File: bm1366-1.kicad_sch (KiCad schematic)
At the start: 56 parts, among them U1 25MHz, U13 ADP171AUJ-R7, U14 BM1366_mode1, U23 ADP171AUJ-R7

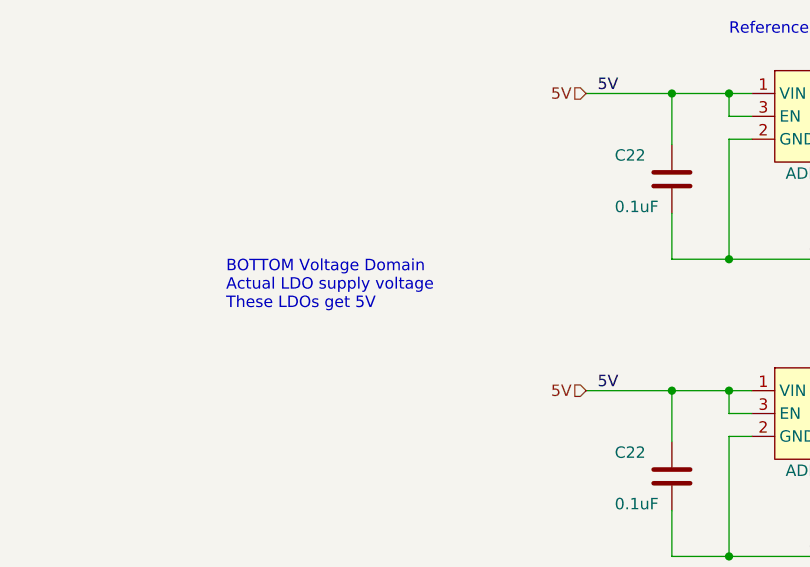
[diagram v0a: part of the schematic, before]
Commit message: add 1v8 LDO and consolidate voltage level translators
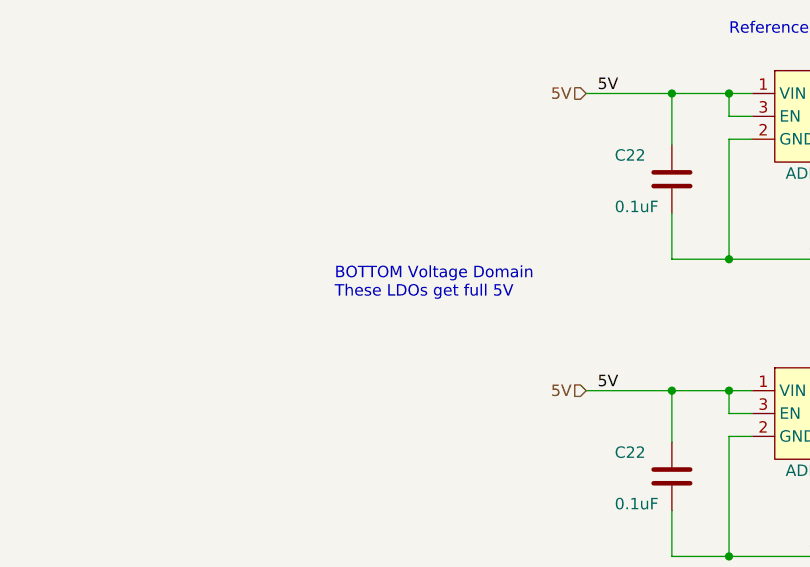
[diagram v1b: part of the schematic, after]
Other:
- note added: "BOTTOM Voltage Domain These LDOs get full 5V"
- note removed: "BOTTOM Voltage Domain Actual LDO supply voltage These LDOs get 5V"
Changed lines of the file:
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@@
     (effects (font (size 1.27 1.27)) (justify left bottom))
   )
-  (text "BOTTOM Voltage Domain\nActual LDO supply voltage\nThese LDOs get 5V"
-    (at 38.1 167.64 0)
+  (text "BOTTOM Voltage Domain\nThese LDOs get full 5V" (at 50.165 166.37 0)
     (effects (font (size 1.27 1.27)) (justify left bottom))
   )

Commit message: Resolved all unconnected pins, re-annotated, reviewed for layout
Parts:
- added TP13 (x4): TestPoint, TestPoint:TestPoint_Pad_D1.5mm, symbol Connector:TestPoint
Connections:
- net TEMP_N1: now also TP13.1
- net TEMP_N2: now also TP13.1
- net TEMP_P1: now also TP13.1
- net TEMP_P2: now also TP13.1
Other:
- moved on the sheet: R6

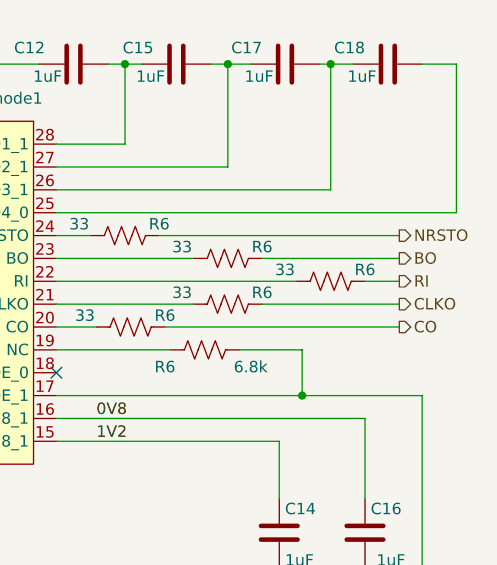
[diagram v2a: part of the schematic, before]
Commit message: replace Q5 with BSS123
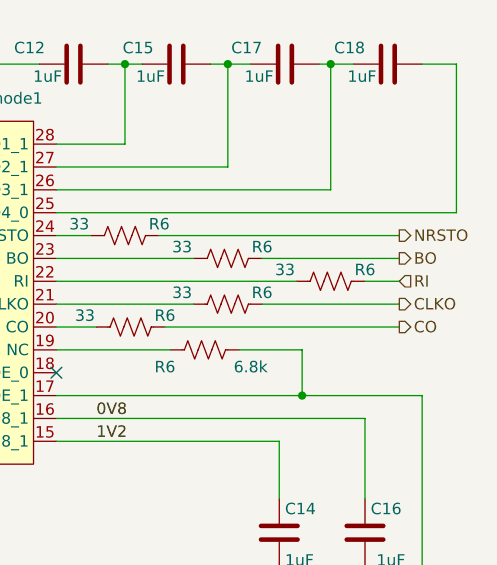
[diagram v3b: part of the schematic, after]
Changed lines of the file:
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@@
     (effects (font (size 1.27 1.27)) (justify right))
   )
-  (hierarchical_label "RI" (shape output) (at 256.54 90.17 0) (fields_autoplaced)
+  (hierarchical_label "RI" (shape input) (at 256.54 90.17 0) (fields_autoplaced)
     (effects (font (size 1.27 1.27)) (justify left))
   )

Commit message: Rough parts placement
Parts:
- TP13: footprint TestPoint:TestPoint_Pad_D1.5mm -> TestPoint:TestPoint_Pad_D1.0mm
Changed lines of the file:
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@@
     (effects (font (size 1.27 1.27)) (justify left bottom))
   )
-  (label "VDD" (at 202.565 66.04 0) (fields_autoplaced)
+  (label "VDD1" (at 202.565 66.04 0) (fields_autoplaced)
     (effects (font (size 1.27 1.27)) (justify left bottom))
   )
@@
     (effects (font (size 1.27 1.27)) (justify left bottom))
   )
-  (label "VDD" (at 74.295 66.04 0) (fields_autoplaced)
+  (label "VDD1" (at 74.295 66.04 0) (fields_autoplaced)
     (effects (font (size 1.27 1.27)) (justify left bottom))
   )
@@
     (effects (font (size 1.27 1.27)) (justify left bottom))
   )
-  (label "VDD" (at 165.735 146.685 0) (fields_autoplaced)
+  (label "VDD1" (at 165.735 146.685 0) (fields_autoplaced)
     (effects (font (size 1.27 1.27)) (justify left bottom))
   )
@@
       (effects (font (size 1.27 1.27)) (justify left) hide)
     )
-    (property "Footprint" "TestPoint:TestPoint_Pad_D1.5mm" (at 136.525 138.43 0)
+    (property "Footprint" "TestPoint:TestPoint_Pad_D1.0mm" (at 136.525 138.43 0)
       (effects (font (size 1.27 1.27)) hide)
     )
@@
       (effects (font (size 1.27 1.27)) (justify left) hide)
     )
-    (property "Footprint" "TestPoint:TestPoint_Pad_D1.5mm" (at 39.37 105.41 0)
+    (property "Footprint" "TestPoint:TestPoint_Pad_D1.0mm" (at 39.37 105.41 0)
       (effects (font (size 1.27 1.27)) hide)
     )
@@
       (effects (font (size 1.27 1.27)) (justify left) hide)
     )
-    (property "Footprint" "TestPoint:TestPoint_Pad_D1.5mm" (at 39.37 102.87 0)
+    (property "Footprint" "TestPoint:TestPoint_Pad_D1.0mm" (at 39.37 102.87 0)
       (effects (font (size 1.27 1.27)) hide)
     )
@@
       (effects (font (size 1.27 1.27)) (justify left) hide)
     )
-    (property "Footprint" "TestPoint:TestPoint_Pad_D1.5mm" (at 171.45 105.41 0)
+    (property "Footprint" "TestPoint:TestPoint_Pad_D1.0mm" (at 171.45 105.41 0)
       (effects (font (size 1.27 1.27)) hide)
     )
@@
       (effects (font (size 1.27 1.27)) (justify left) hide)
     )
-    (property "Footprint" "TestPoint:TestPoint_Pad_D1.5mm" (at 171.45 102.87 0)
+    (property "Footprint" "TestPoint:TestPoint_Pad_D1.0mm" (at 171.45 102.87 0)
       (effects (font (size 1.27 1.27)) hide)
     )
@@
       (effects (font (size 1.27 1.27)) (justify left) hide)
     )
-    (property "Footprint" "TestPoint:TestPoint_Pad_D1.5mm" (at 136.525 171.45 0)
-      (effects (font (size 1.27 1.27)) hide)
-    )
+    (property "Footprint" "TestPoint:TestPoint_Pad_D1.0mm" (at 136.525 171.45 0)
+      (effects (font (size 1.27 1.27)) hide)
+    )

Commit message: more parts placement
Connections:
- net CLKI: no longer U14.8 (CLKI)
- net BI1: now reaches R6.2, U14.6 (BI)
- net TEMP_N1 renamed TEMP_N1_1
- net TEMP_N2 renamed TEMP_N2_1
- net TEMP_P1 renamed TEMP_P1_1
- net TEMP_P2 renamed TEMP_P2_1
- new net CLKI1: U14.8 (CLKI)
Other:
- moved on the sheet: TP13
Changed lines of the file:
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@@
+    (stroke (width 0) (type default))
+  )
+  (wire (pts (xy 167.64 100.33) (xy 182.88 100.33))
     (stroke (width 0) (type default))
   )
@@
     (stroke (width 0) (type default))
   )
-  (wire (pts (xy 171.45 100.33) (xy 182.88 100.33))
-    (stroke (width 0) (type default))
-  )
   (wire (pts (xy 116.84 181.61) (xy 118.745 181.61))
     (stroke (width 0) (type default))
@@
     (stroke (width 0) (type default))
   )
+  (wire (pts (xy 167.64 97.79) (xy 182.88 97.79))
+    (stroke (width 0) (type default))
+  )
   (wire (pts (xy 116.84 66.04) (xy 119.38 66.04))
     (stroke (width 0) (type default))
@@
     (stroke (width 0) (type default))
   )
-  (wire (pts (xy 171.45 97.79) (xy 182.88 97.79))
-    (stroke (width 0) (type default))
-  )
   (wire (pts (xy 93.98 146.05) (xy 93.98 143.51))
     (stroke (width 0) (type default))
@@
     (effects (font (size 1.27 1.27)) (justify left bottom))
   )
-  (label "RO" (at 41.275 90.17 0) (fields_autoplaced)
+  (label "RO1" (at 41.275 90.17 0) (fields_autoplaced)
+    (effects (font (size 1.27 1.27)) (justify left bottom))
+  )
+  (label "BI1" (at 41.275 87.63 0) (fields_autoplaced)
     (effects (font (size 1.27 1.27)) (justify left bottom))
   )
@@
     (effects (font (size 1.27 1.27)) (justify left bottom))
   )
-  (label "CLKI" (at 41.275 92.71 0) (fields_autoplaced)
+  (label "CLKI1" (at 41.275 92.71 0) (fields_autoplaced)
     (effects (font (size 1.27 1.27)) (justify left bottom))
   )
@@
     (effects (font (size 1.27 1.27)) (justify left bottom))
   )
-  (label "TEMP_N1" (at 41.275 100.33 0) (fields_autoplaced)
+  (label "TEMP_N1_1" (at 41.275 100.33 0) (fields_autoplaced)
     (effects (font (size 1.27 1.27)) (justify left bottom))
   )
@@
     (effects (font (size 1.27 1.27)) (justify left bottom))
   )
-  (label "TEMP_P2" (at 172.72 97.79 0) (fields_autoplaced)
+  (label "TEMP_P2_1" (at 169.545 97.79 0) (fields_autoplaced)
     (effects (font (size 1.27 1.27)) (justify left bottom))
   )
@@
     (effects (font (size 1.27 1.27)) (justify left bottom))
   )
-  (label "TEMP_P1" (at 41.275 97.79 0) (fields_autoplaced)
+  (label "TEMP_P1_1" (at 41.275 97.79 0) (fields_autoplaced)
     (effects (font (size 1.27 1.27)) (justify left bottom))
   )
@@
     (effects (font (size 1.27 1.27)) (justify left bottom))
   )
-  (label "TEMP_N2" (at 172.72 100.33 0) (fields_autoplaced)
-    (effects (font (size 1.27 1.27)) (justify left bottom))
-  )
-  (label "CI" (at 41.275 95.25 0) (fields_autoplaced)
+  (label "TEMP_N2_1" (at 169.545 100.33 0) (fields_autoplaced)
+    (effects (font (size 1.27 1.27)) (justify left bottom))
+  )
+  (label "CI1" (at 41.275 95.25 0) (fields_autoplaced)
     (effects (font (size 1.27 1.27)) (justify left bottom))
   )
@@
     )
   )
-  (symbol (lib_id "Connector:TestPoint") (at 171.45 100.33 90) (mirror x) (unit 1)
+  (symbol (lib_id "Connector:TestPoint") (at 167.64 100.33 90) (mirror x) (unit 1)
     (in_bom no) (on_board yes) (dnp no)
-    (property "Reference" "TP13" (at 165.1 100.33 90)
-      (effects (font (size 1.27 1.27)))
-    )
-    (property "Value" "TestPoint" (at 165.735 101.5999 90)
+    (property "Reference" "TP13" (at 161.29 100.33 90)
+      (effects (font (size 1.27 1.27)))
+    )
+    (property "Value" "TestPoint" (at 161.925 101.5999 90)
       (effects (font (size 1.27 1.27)) (justify left) hide)
     )
-    (property "Footprint" "TestPoint:TestPoint_Pad_D1.0mm" (at 171.45 105.41 0)
-      (effects (font (size 1.27 1.27)) hide)
-    )
-    (property "Datasheet" "~" (at 171.45 105.41 0)
+    (property "Footprint" "TestPoint:TestPoint_Pad_D1.0mm" (at 167.64 105.41 0)
+      (effects (font (size 1.27 1.27)) hide)
+    )
+    (property "Datasheet" "~" (at 167.64 105.41 0)
       (effects (font (size 1.27 1.27)) hide)
     )
@@
     )
   )
-  (symbol (lib_id "Connector:TestPoint") (at 171.45 97.79 90) (mirror x) (unit 1)
+  (symbol (lib_id "Connector:TestPoint") (at 167.64 97.79 90) (mirror x) (unit 1)
     (in_bom no) (on_board yes) (dnp no)
-    (property "Reference" "TP13" (at 165.1 97.79 90)
-      (effects (font (size 1.27 1.27)))
-    )
-    (property "Value" "TestPoint" (at 165.735 99.0599 90)
+    (property "Reference" "TP13" (at 161.29 97.79 90)
+      (effects (font (size 1.27 1.27)))
+    )
+    (property "Value" "TestPoint" (at 161.925 99.0599 90)
       (effects (font (size 1.27 1.27)) (justify left) hide)
     )
-    (property "Footprint" "TestPoint:TestPoint_Pad_D1.0mm" (at 171.45 102.87 0)
-      (effects (font (size 1.27 1.27)) hide)
-    )
-    (property "Datasheet" "~" (at 171.45 102.87 0)
-      (effects (font (size 1.27 1.27)) hide)
-    )
+    (property "Footprint" "TestPoint:TestPoint_Pad_D1.0mm" (at 167.64 102.87 0)
+      (effects (font (size 1.27 1.27)) hide)
+    )
+    (property "Datasheet" "~" (at 167.64 102.87 0)
+      (effects (font (size 1.27 1.27)) hide)
+    )

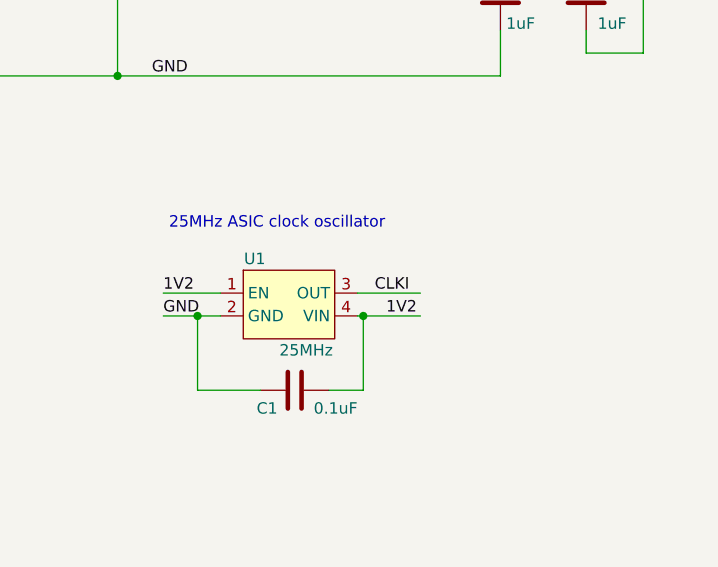
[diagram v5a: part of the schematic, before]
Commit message: add some power planes and do some comms routing
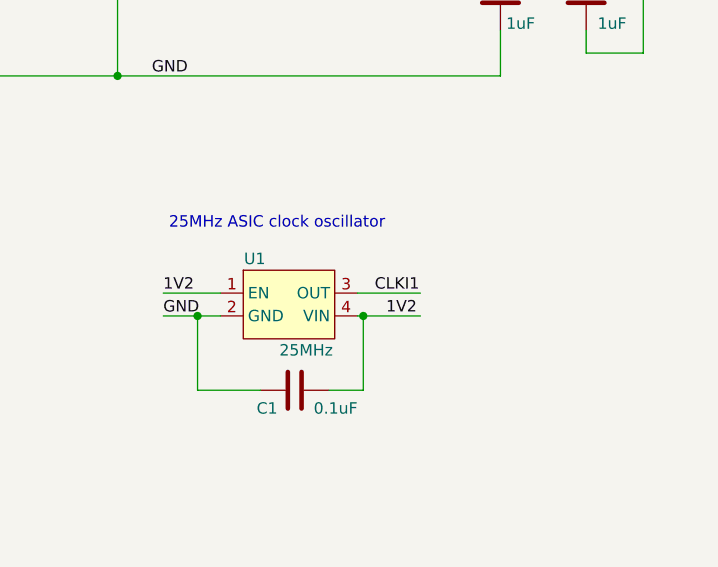
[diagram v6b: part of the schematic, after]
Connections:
- net CLKI is gone; now on net CLKI1: U1.3 (OUT)
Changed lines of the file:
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@@
     (effects (font (size 1.27 1.27)) (justify left bottom))
   )
-  (label "CLKI" (at 229.235 151.13 0) (fields_autoplaced)
+  (label "CLKI1" (at 229.235 151.13 0) (fields_autoplaced)
     (effects (font (size 1.27 1.27)) (justify left bottom))
   )

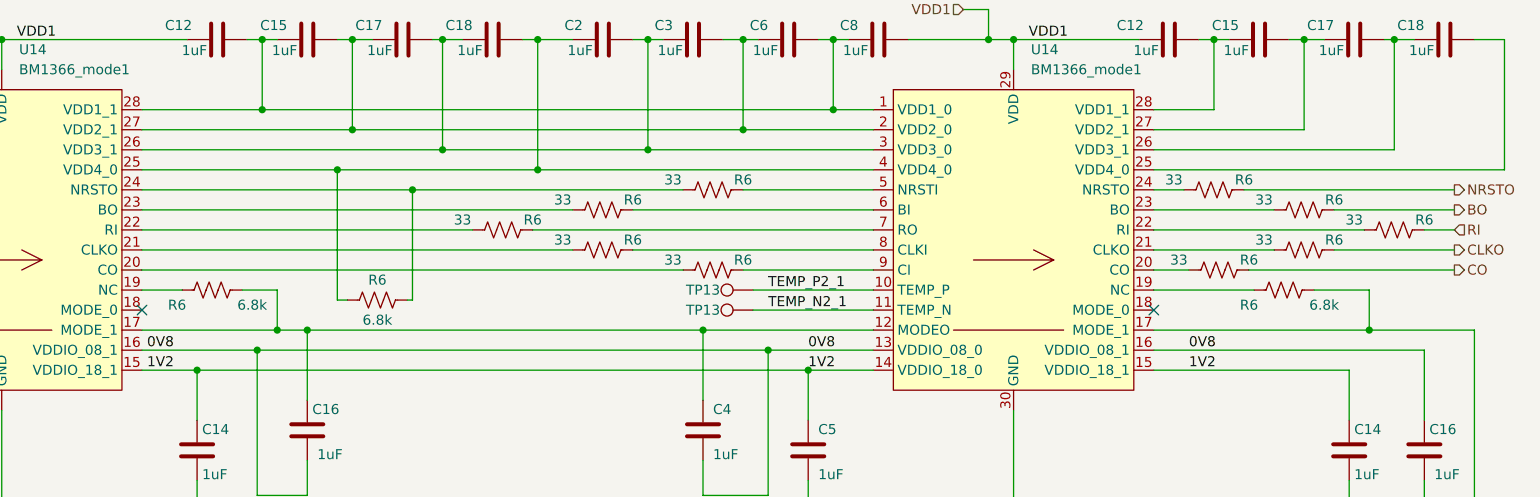
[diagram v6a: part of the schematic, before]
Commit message: shuffle resistors on RI/RO, more routing on ASICs
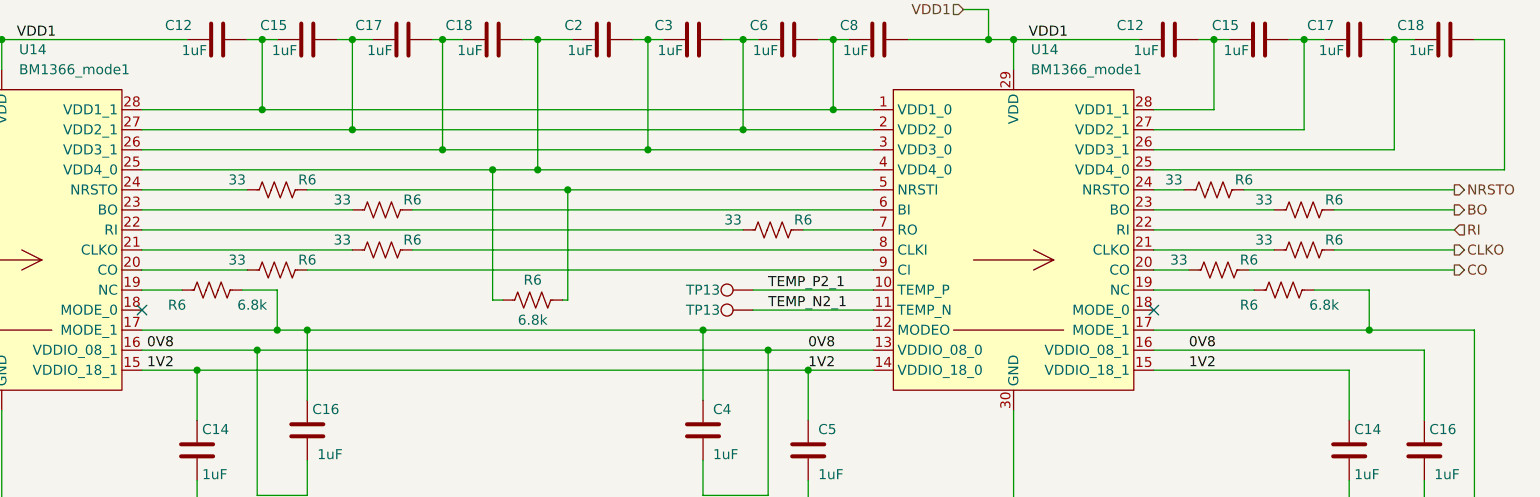
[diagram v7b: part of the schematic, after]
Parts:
- removed R6 (x3): 33, Resistor_SMD:R_0402_1005Metric, symbol Device:R_US
- added R6 (x2): 33, Resistor_SMD:R_0402_1005Metric, symbol Device:R_US
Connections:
- net RI: now also U14.22 (RI)
- net at U14.20 (CO): now also R6.1
- net at U14.24 (NRSTO): now also R6.1; no longer R6.2
- net at U14.9 (CI): now also R6.2
- net at U14.5 (NRSTI): now also R6.2, R6.2
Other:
- moved on the sheet: R6

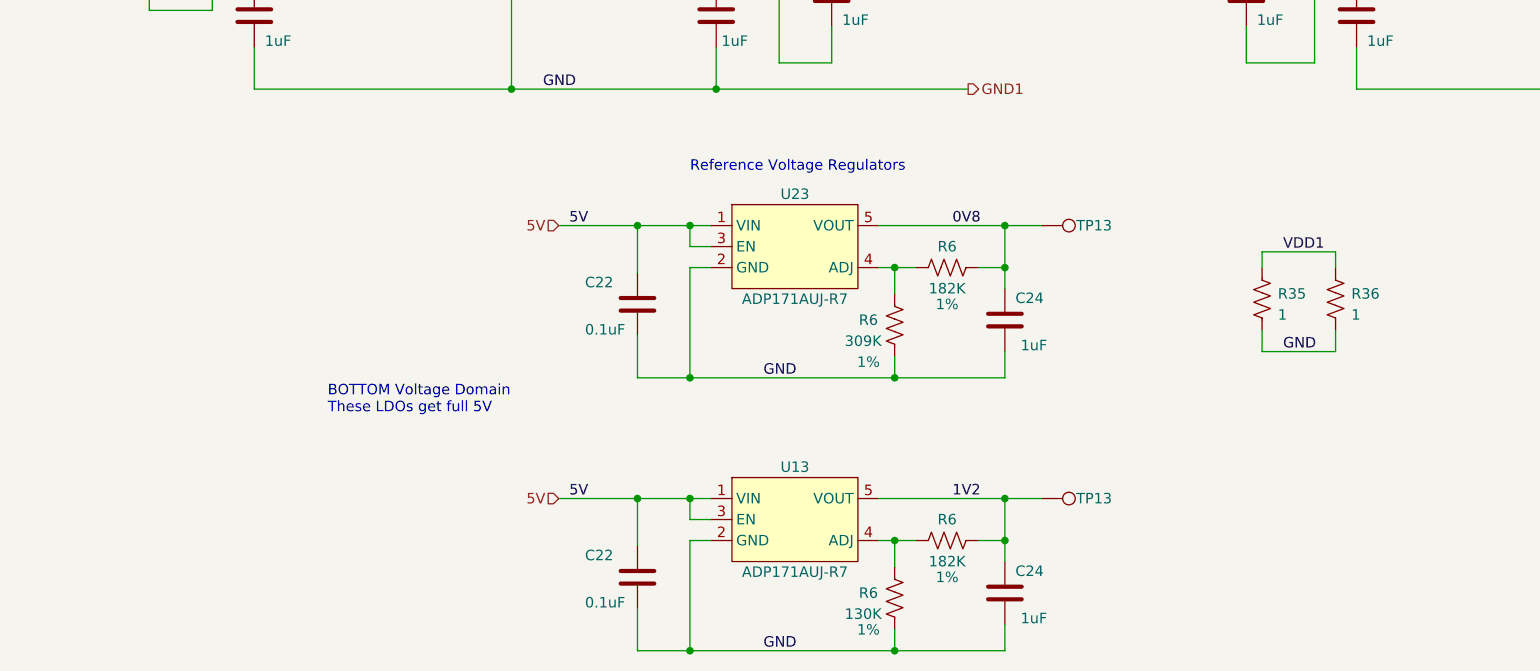
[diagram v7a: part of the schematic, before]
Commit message: add oscillators, large bypass caps, start routing reference voltages
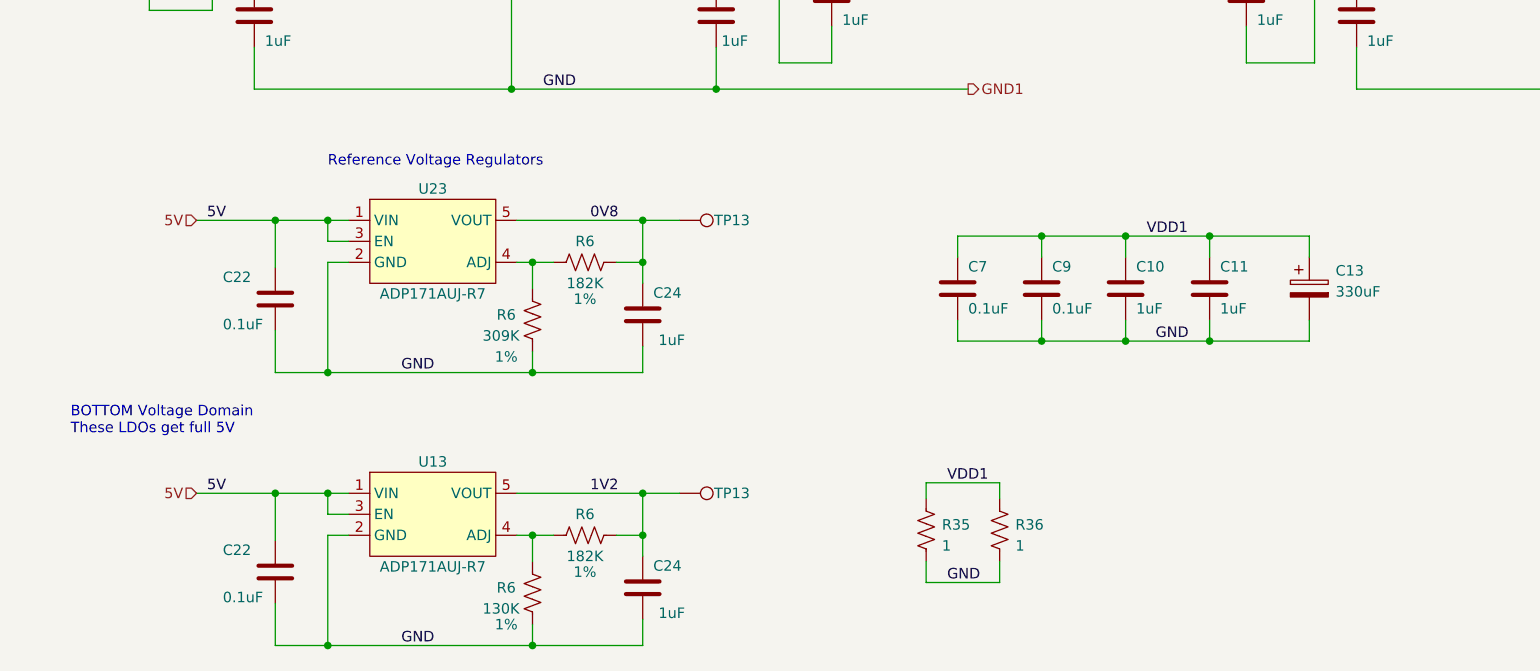
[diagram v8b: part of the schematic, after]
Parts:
- added C10, C11: 1uF, Capacitor_SMD:C_0402_1005Metric, symbol Device:C
- added C13: 330uF, Capacitor_Tantalum_SMD:CP_EIA-7343-31_Kemet-D_Pad2.25x2.55mm_HandSolder, symbol Device:C_Polarized
- added C7, C9: 0.1uF, Capacitor_SMD:C_0402_1005Metric, symbol Device:C
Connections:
- net GND1: now also C10.2, C11.2, C13.2, C7.2, C9.2
- net VDD1: now also C10.1, C11.1, C13.1, C7.1, C9.1
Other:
- moved on the sheet: C22, C24, R35, R36, R6, TP13, U13, U23
